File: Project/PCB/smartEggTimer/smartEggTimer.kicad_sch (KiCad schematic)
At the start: 61 parts, among them J1 Conn_01x05_Pin, J2 Conn_01x02_Pin, J3 Conn_01x02_Pin, J4 Conn_01x02_Pin, J5 Conn_01x02_Socket, J6 Conn_01x02_Socket, J8 Conn_01x02_Pin, Q1 Q_PMOS_DGS, SW1 SW_Push_Dual, SW2 RotaryEncoder, SW3 SW_Push_Dual, SW4 SW_Push_Dual, SW5 SW_Push_Dual, SW6 SW_Push_Dual, SW7 SW_SPDT, U1 STM32F103RET6, U2 XC6206P332MR-G

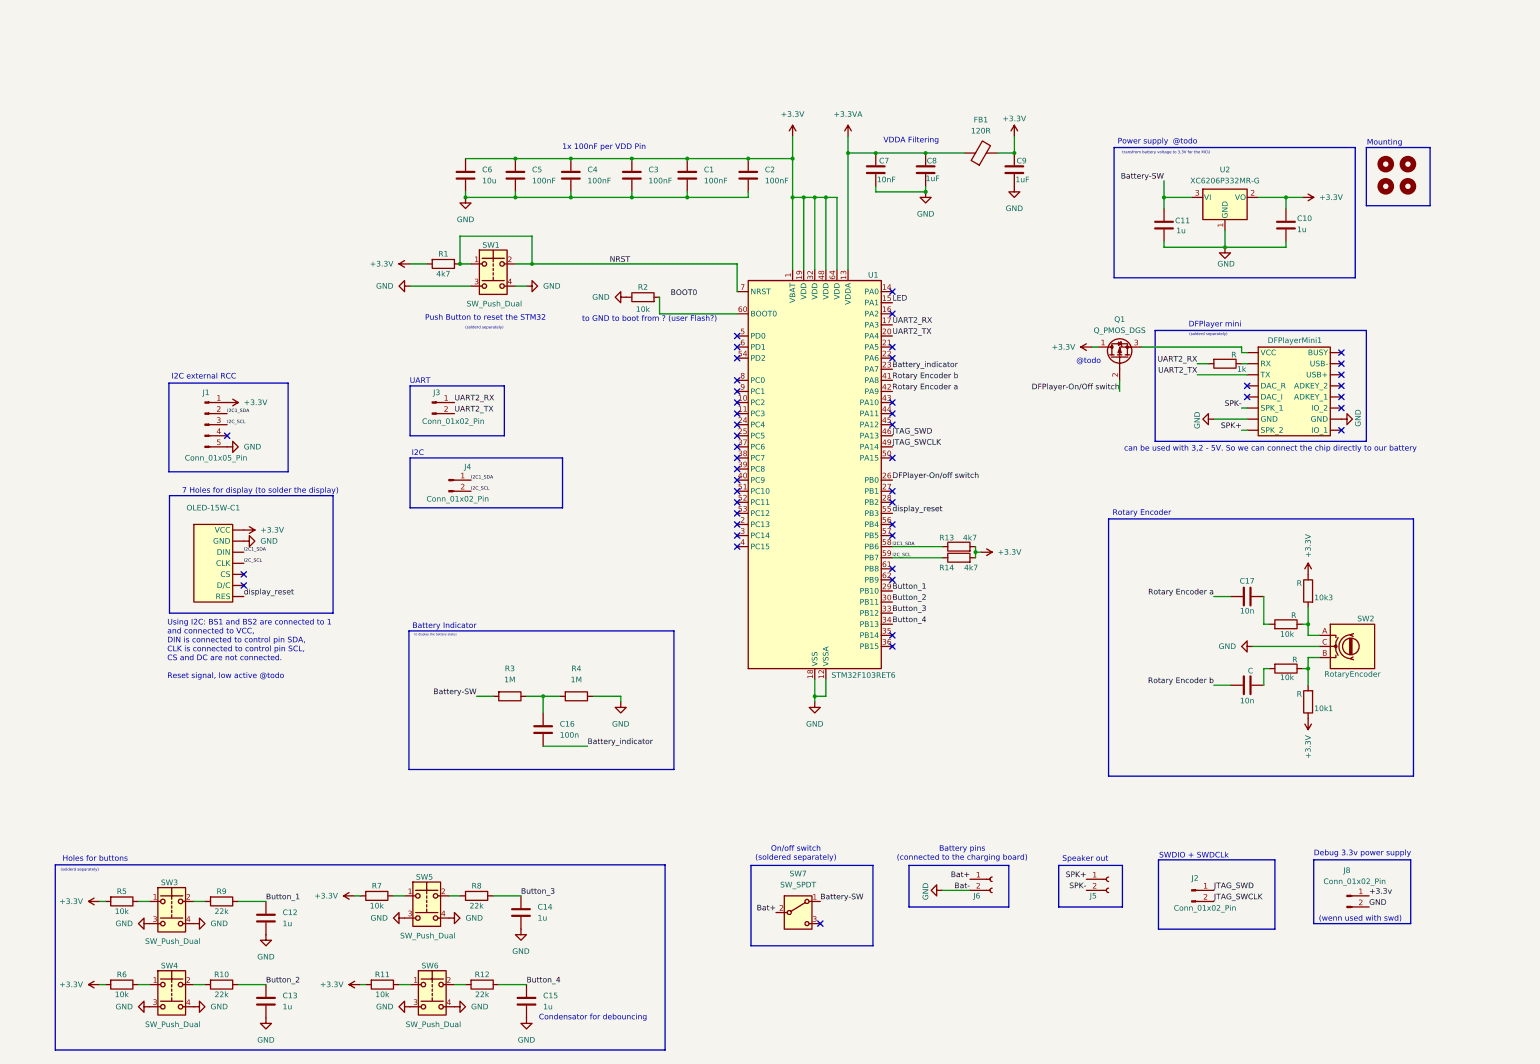
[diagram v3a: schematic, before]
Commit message: fix annotation, add resistor to mosfet, remove debug power supply, use new voltage regulator and choose footprints
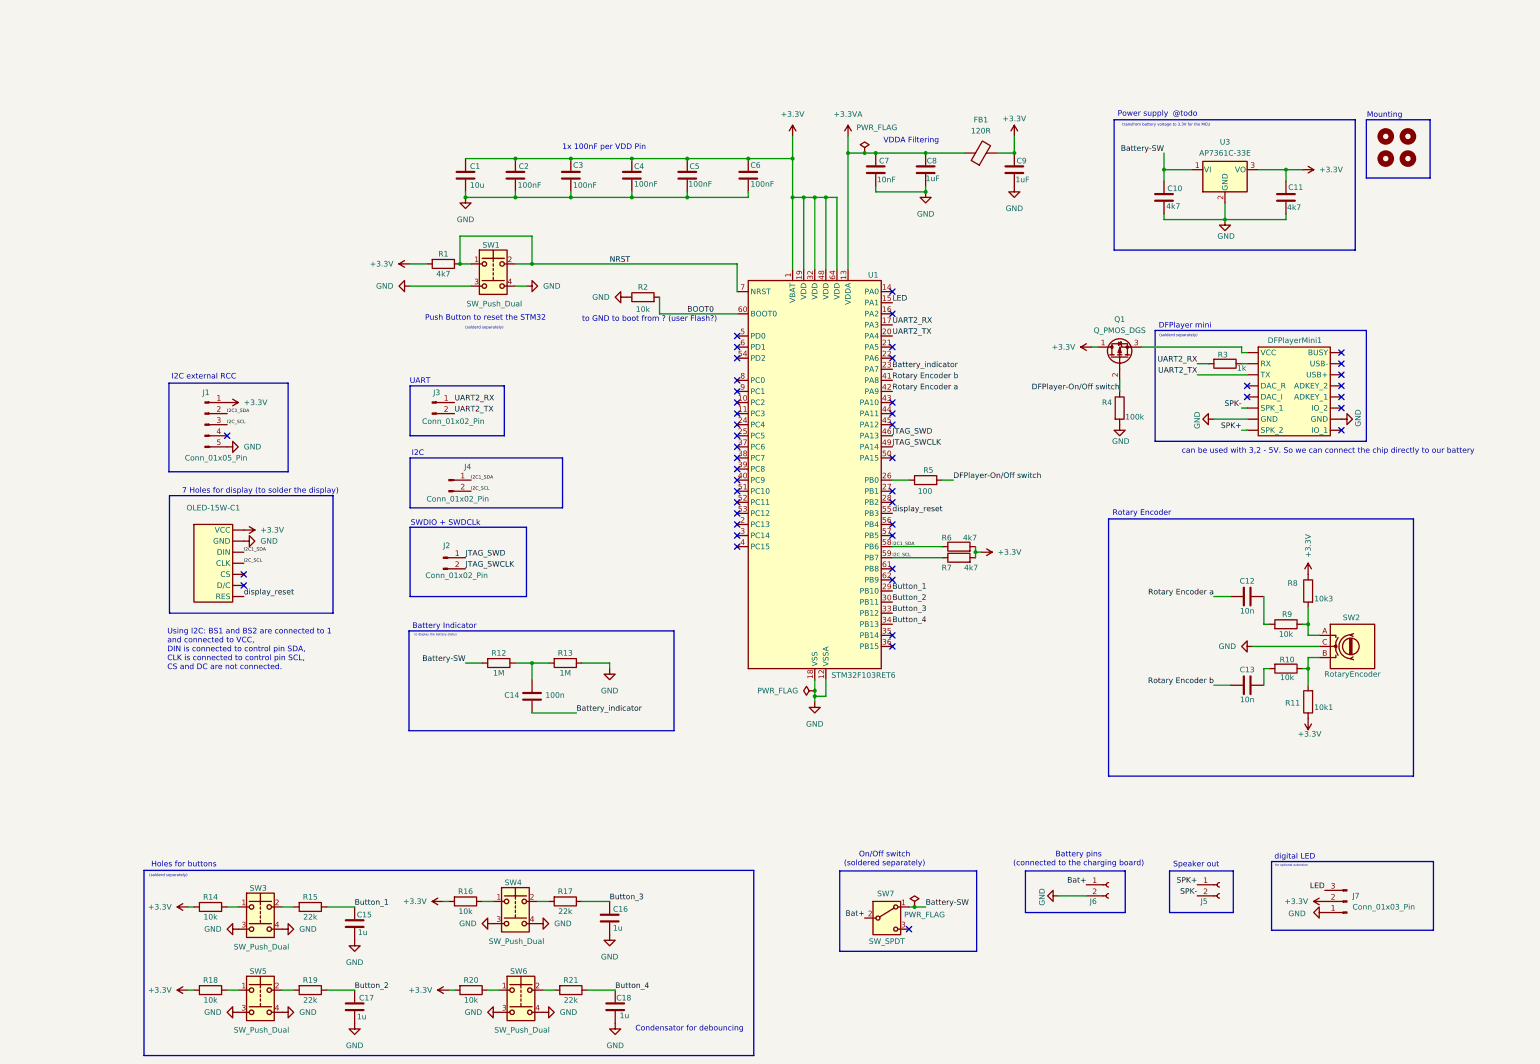
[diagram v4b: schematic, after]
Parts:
- removed J8: Conn_01x02_Pin, Connector_PinHeader_2.54mm:PinHeader_1x01_P2.54mm_Vertical, symbol Connector:Conn_01x02_Pin
- removed U2: XC6206P332MR-G, Package_TO_SOT_SMD:SOT-23-3, symbol Regulator_Linear:XC6206PxxxMR
- added J7: Conn_01x03_Pin, Connector_PinHeader_2.54mm:PinHeader_1x03_P2.54mm_Vertical, symbol Connector:Conn_01x03_Pin
- added R4: 100k, Resistor_SMD:R_0402_1005Metric, symbol Device:R
- added R5: 100, Resistor_SMD:R_0402_1005Metric, symbol Device:R
- added U3: AP7361C-33E, Package_TO_SOT_SMD:SOT-223-3_TabPin2, symbol Regulator_Linear:AP7361C-33E
- C10: renamed from C11; value 1u -> 4k7
- C11: renamed from C10; value 1u -> 4k7
- C12: renamed from C17; footprint (none) -> Capacitor_SMD:C_0805_2012Metric
- C13: renamed from 10n; value C -> 10n; footprint (none) -> Capacitor_SMD:C_0805_2012Metric
- C14: renamed from C16; footprint (none) -> Capacitor_SMD:C_0402_1005Metric
- C15: renamed from C12; footprint (none) -> Capacitor_SMD:C_0603_1608Metric
- C16: renamed from C14; footprint (none) -> Capacitor_SMD:C_0603_1608Metric
- C17: renamed from C13; footprint (none) -> Capacitor_SMD:C_0603_1608Metric
- C18: renamed from C15; footprint (none) -> Capacitor_SMD:C_0603_1608Metric
- FB1: footprint (none) -> Inductor_SMD:L_Chilisin_BMRB00050518
- H1, H2: footprint (none) -> MountingHole:MountingHole_4.3mm_M4
- H3, H8: footprint (none) -> MountingHole:MountingHole_4.3mm_M4_DIN965
- J5, J6: footprint (none) -> Connector_PinHeader_2.54mm:PinHeader_1x02_P2.54mm_Vertical
- Q1: footprint (none) -> Package_TO_SOT_THT:TO-220-3_Vertical
- R1, R2: footprint (none) -> Resistor_SMD:R_0402_1005Metric
- R10, R9: renamed from 10k; value R -> 10k; footprint (none) -> Resistor_SMD:R_0402_1005Metric
- R11: renamed from 10k1; value R -> 10k1; footprint (none) -> Resistor_SMD:R_0402_1005Metric
- R12: renamed from R3; footprint (none) -> Resistor_SMD:R_0402_1005Metric
- R13: renamed from R4; footprint (none) -> Resistor_SMD:R_0402_1005Metric
- R14: renamed from R5; footprint (none) -> Resistor_SMD:R_0402_1005Metric
- R15: renamed from R9; footprint (none) -> Resistor_SMD:R_0402_1005Metric
- R16: renamed from R7; footprint (none) -> Resistor_SMD:R_0402_1005Metric
- R17: renamed from R8; footprint (none) -> Resistor_SMD:R_0402_1005Metric
- R18: renamed from R6; footprint (none) -> Resistor_SMD:R_0402_1005Metric
- R19: renamed from R10; footprint (none) -> Resistor_SMD:R_0402_1005Metric
- R20: renamed from R11; footprint (none) -> Resistor_SMD:R_0402_1005Metric
- R21: renamed from R12; footprint (none) -> Resistor_SMD:R_0402_1005Metric
- R3: renamed from 1k; value R -> 1k; footprint (none) -> Resistor_SMD:R_0402_1005Metric
- R6: renamed from R13; footprint (none) -> Resistor_SMD:R_0402_1005Metric
- R7: renamed from R14; footprint (none) -> Resistor_SMD:R_0402_1005Metric
- R8: renamed from 10k3; value R -> 10k3; footprint (none) -> Resistor_SMD:R_0402_1005Metric
- SW1: footprint (none) -> Button_Switch_THT:SW_PUSH_6mm_H9.5mm
- SW2: footprint (none) -> Rotary_Encoder:RotaryEncoder_Alps_EC12E_Vertical_H20mm
- SW3, SW6: footprint (none) -> Button_Switch_THT:SW_PUSH_6mm_H13mm
- SW4: renamed from SW5; footprint (none) -> Button_Switch_THT:SW_PUSH_6mm_H13mm
- SW5: renamed from SW4; footprint (none) -> Button_Switch_THT:SW_PUSH_6mm_H13mm
- SW7: footprint (none) -> Button_Switch_THT:SW_Slide_SPDT_Angled_CK_OS102011MA1Q
- renumbered C6 to C1, C5 to C2, C4 to C3, C3 to C4, C1 to C5, C2 to C6
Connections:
- net +3.3V: now also J7.2 (Pin_2), U3.3 (VO)
- net BOOT0: now also R2.2, U1.60 (BOOT0)
- net Battery-SW: now also U3.1 (VI)
- net DFPlayer-On/Off switch: now also R4.1, R5.2
- net GND: now also J7.1 (Pin_1), R4.2, U3.2 (GND)
- net LED: now also J7.3 (Pin_3)
- net DFPlayer-On/off switch: no longer names the net of U1.26 (PB0)
- net DFPlayer-On/off switch: now also R5.1
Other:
- note added: "On/Off switch (soldered separately)"
- note added: "Using I2C: BS1 and BS2 are connected to 1 and connected to VCC, DIN is connected to control pin SDA, CLK is connected to control pin SCL, CS and DC are not connected."
- note added: "digital LED"
- note added: "for optional extension"
- note removed: "(wenn used with swd)"
- note removed: "Debug 3.3v power supply"
- note removed: "On/off switch (soldered separately)"
- note removed: "Using I2C: BS1 and BS2 are connected to 1 and connected to VCC, DIN is connected to control pin SDA, CLK is connected to control pin SCL, CS and DC are not connected. Reset signal, low active @todo"
- moved on the sheet: C10, C11, C14, C15, C16, C17, C18, J2, J5, J6, R12, R13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

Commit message: cosmetic improvements
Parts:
- C2, C3, C4, C5, C6: value 100nF -> 100n
- C7: value 10nF -> 10n
- C8, C9: value 1uF -> 1u
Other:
- note added: "to GND to boot from main flash memory"
- note removed: "to GND to boot from ? (user Flash?)"
- moved on the sheet: J2
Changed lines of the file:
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@@
 	)
 	(rectangle
-		(start 100.33 132.715)
-		(end 127 148.59)
+		(start 100.33 133.985)
+		(end 127 149.86)
 		(stroke
 			(width 0)
@@
 		)
 	)
-	(text "to GND to boot from ? (user Flash?)"
+	(text "to GND to boot from main flash memory"
 		(exclude_from_sim no)
-		(at 155.194 85.09 0)
+		(at 161.036 85.09 0)
 		(effects
 			(font
-				(size 1.27 1.27)
+				(size 1 1)
 			)
 		)
@@
 	(text "SWDIO + SWDCLk"
 		(exclude_from_sim no)
-		(at 108.458 131.826 0)
+		(at 108.458 133.096 0)
 		(effects
 			(font
@@
 	)
 	(label "JTAG_SWCLK"
-		(at 113.03 142.24 0)
+		(at 113.03 143.51 0)
 		(fields_autoplaced yes)
 		(effects
@@
 	)
 	(label "JTAG_SWD"
-		(at 113.03 139.7 0)
+		(at 113.03 140.97 0)
 		(fields_autoplaced yes)
 		(effects
@@
 	(symbol
 		(lib_id "Connector:Conn_01x02_Pin")
-		(at 107.95 139.7 0)
+		(at 107.95 140.97 0)
 		(unit 1)
 		(exclude_from_sim no)
@@
 		(dnp no)
 		(property "Reference" "J2"
-			(at 108.712 136.906 0)
+			(at 108.966 139.446 0)
 			(effects
 				(font
@@
 		)
 		(property "Value" "Conn_01x02_Pin"
-			(at 110.998 143.764 0)
+			(at 110.998 145.034 0)
 			(effects
 				(font
@@
 		)
 		(property "Footprint" "Connector_PinHeader_2.54mm:PinHeader_1x01_P2.54mm_Vertical"
-			(at 107.95 139.7 0)
+			(at 107.95 140.97 0)
 			(effects
 				(font
@@
 		)
 		(property "Datasheet" "~"
-			(at 107.95 139.7 0)
+			(at 107.95 140.97 0)
 			(effects
 				(font
@@
 		)
 		(property "Description" "Generic connector, single row, 01x02, script generated"
-			(at 107.95 139.7 0)
+			(at 107.95 140.97 0)
 			(effects
 				(font
@@
 		(dnp no)
 		(property "Reference" "J4"
-			(at 113.538 118.872 0)
+			(at 109.982 120.396 0)
 			(effects
 				(font
@@
 			)
 		)
-		(property "Value" "1uF"
+		(property "Value" "1u"
 			(at 218.44 52.832 0)
 			(effects
@@
 		(on_board yes)
 		(dnp no)
-		(fields_autoplaced yes)
 		(property "Reference" "OLED-15W-C1"
-			(at 55.245 128.27 0)
+			(at 54.61 130.048 0)
 			(effects
 				(font
@@
 			)
 		)
-		(property "Value" "100nF"
+		(property "Value" "100n"
 			(at 124.968 54.356 0)
 			(effects
@@
 			)
 		)
-		(property "Value" "100nF"
+		(property "Value" "100n"
 			(at 137.668 54.356 0)
 			(effects
@@
 			)
 		)
-		(property "Value" "10nF"
+		(property "Value" "10n"
 			(at 207.264 53.086 0)
 			(effects
@@
 		(dnp no)
 		(property "Reference" "J3"
-			(at 106.426 101.854 0)
+			(at 106.172 102.362 0)
 			(effects
 				(font
@@
 			)
 		)
-		(property "Value" "1uF"
+		(property "Value" "1u"
 			(at 239.014 53.086 0)
 			(effects
@@
 			)
 		)
-		(property "Value" "100nF"
+		(property "Value" "100n"
 			(at 178.308 54.102 0)
 			(effects
@@
 			)
 		)
-		(property "Value" "100nF"
+		(property "Value" "100n"
 			(at 164.084 54.102 0)
 			(effects
@@
 			)
 		)
-		(property "Value" "100nF"
+		(property "Value" "100n"
 			(at 151.638 54.102 0)
 			(effects

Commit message: minor fixes
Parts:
- FB1: footprint Inductor_SMD:L_Chilisin_BMRB00050518 -> Inductor_SMD:L_0603_1608Metric
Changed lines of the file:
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@@
 			)
 		)
-		(property "Footprint" "Inductor_SMD:L_Chilisin_BMRB00050518"
+		(property "Footprint" "Inductor_SMD:L_0603_1608Metric"
 			(at 231.14 48.768 90)
 			(effects
